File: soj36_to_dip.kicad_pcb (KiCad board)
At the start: 4 copper layers, 18 x 41.9 mm, 3 parts, among them U1 IS61C5128AL-10KLI, U2 AS6C4008-55PCN

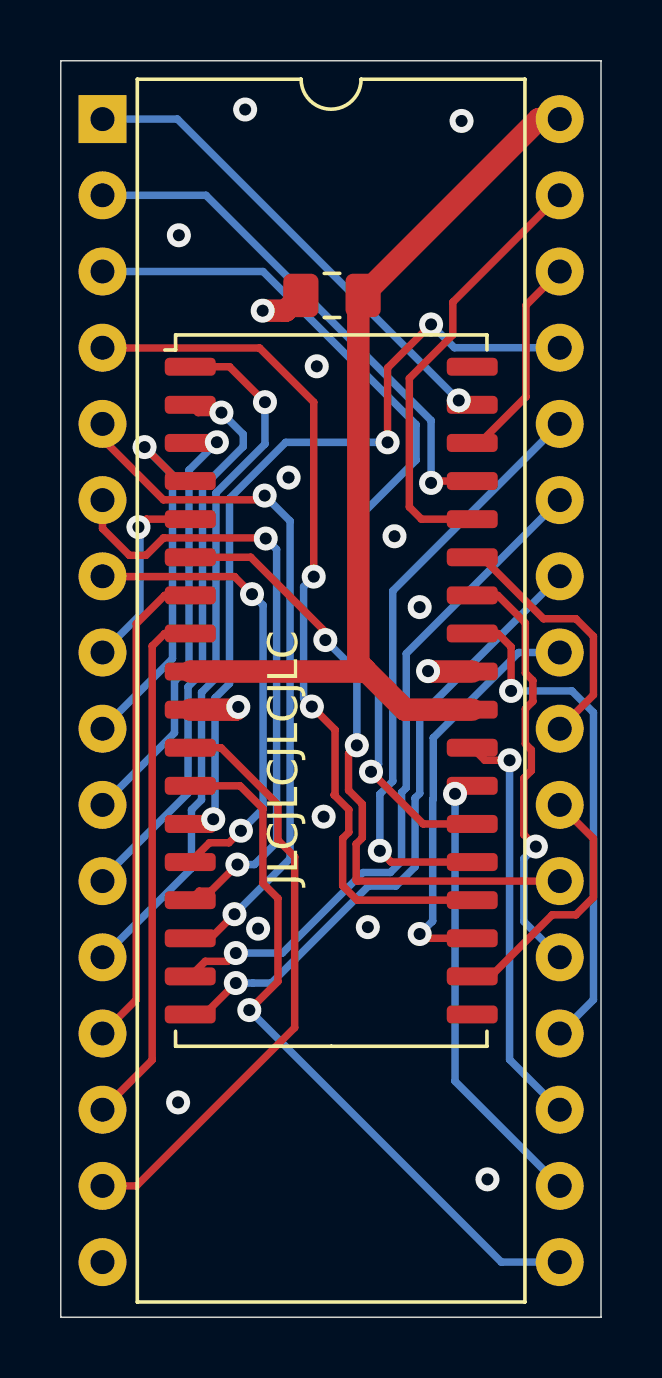
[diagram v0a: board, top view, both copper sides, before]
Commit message: Update for KiCad 6
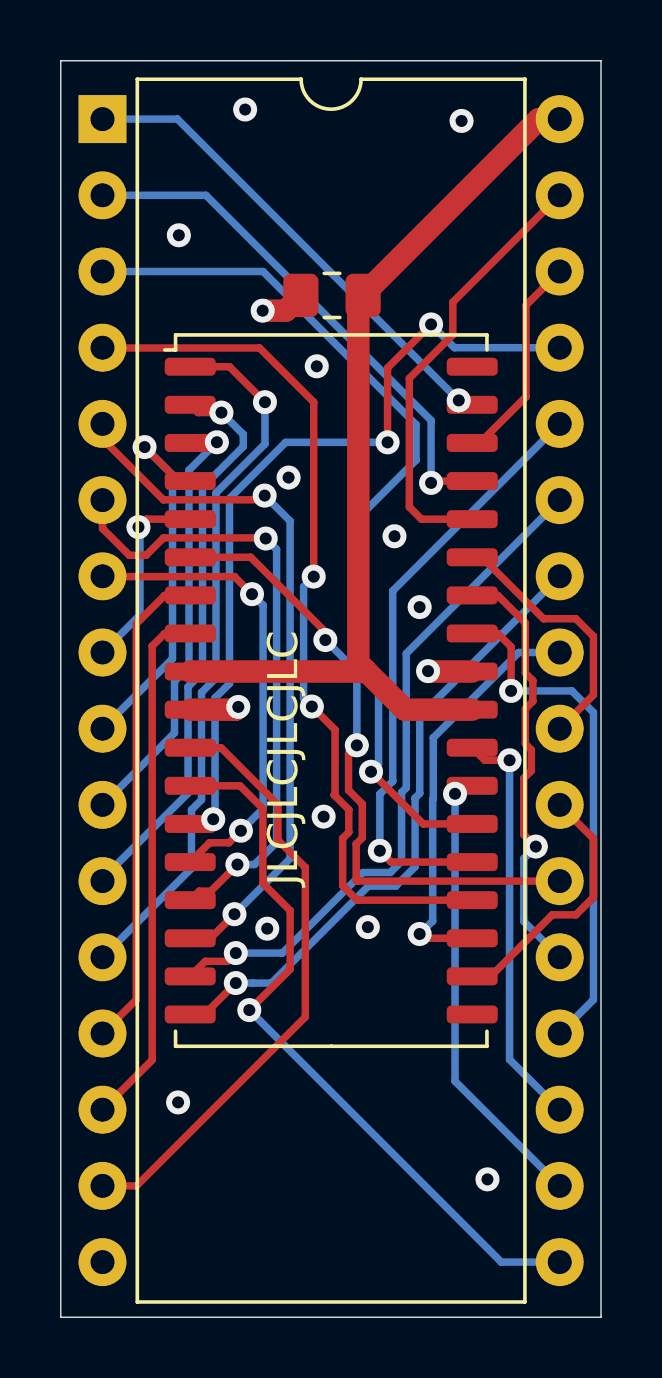
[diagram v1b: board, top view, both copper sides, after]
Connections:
- net ~CE renamed ~{CE}
- net ~OE renamed ~{OE}
- net ~WE renamed ~{WE}
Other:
- net class Default removed
